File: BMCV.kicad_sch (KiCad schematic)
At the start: 30 parts, among them J13 DebugPins, J14 USB_C_Receptacle_USB2.0_14P, SW14 Reset, SW15 Boot, U32 TXS0108EPW, U36 STM32G474CETx, Y1 38.4MHz 10pF

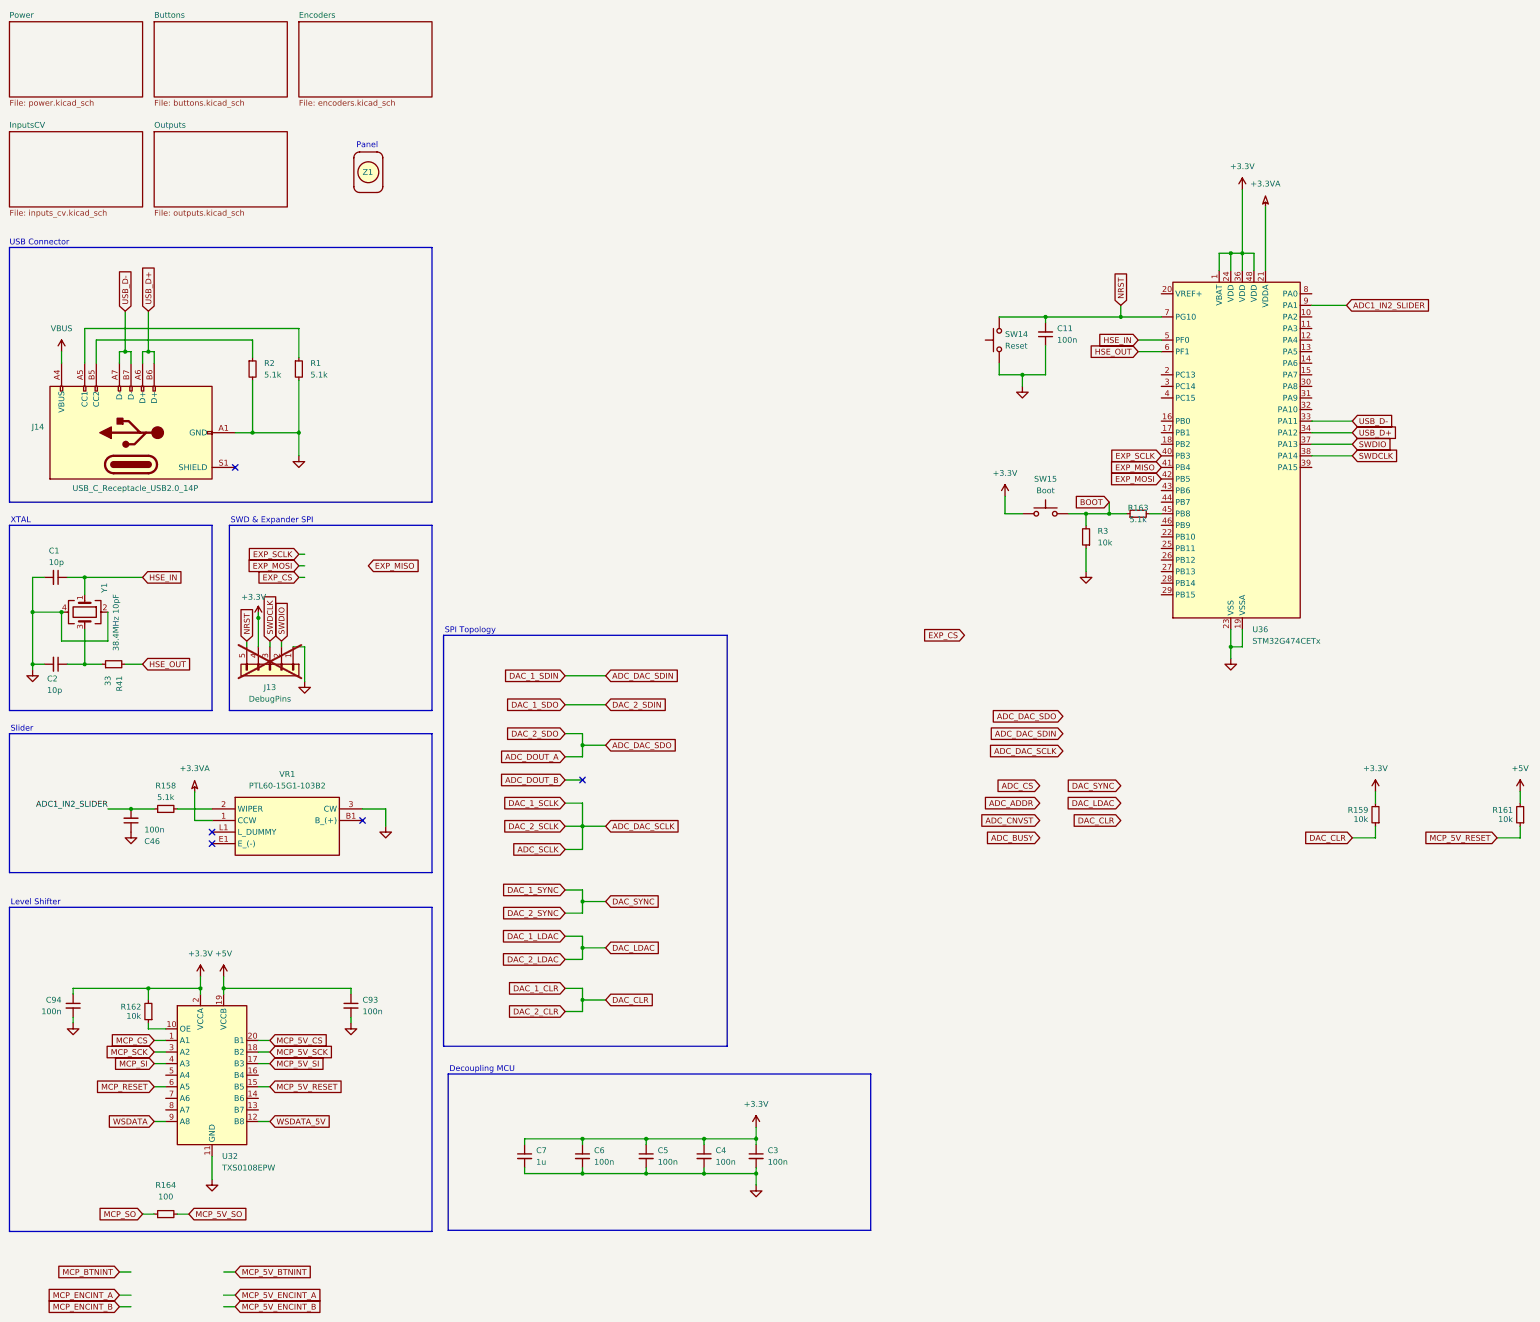
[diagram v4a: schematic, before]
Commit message: switches & led data routing
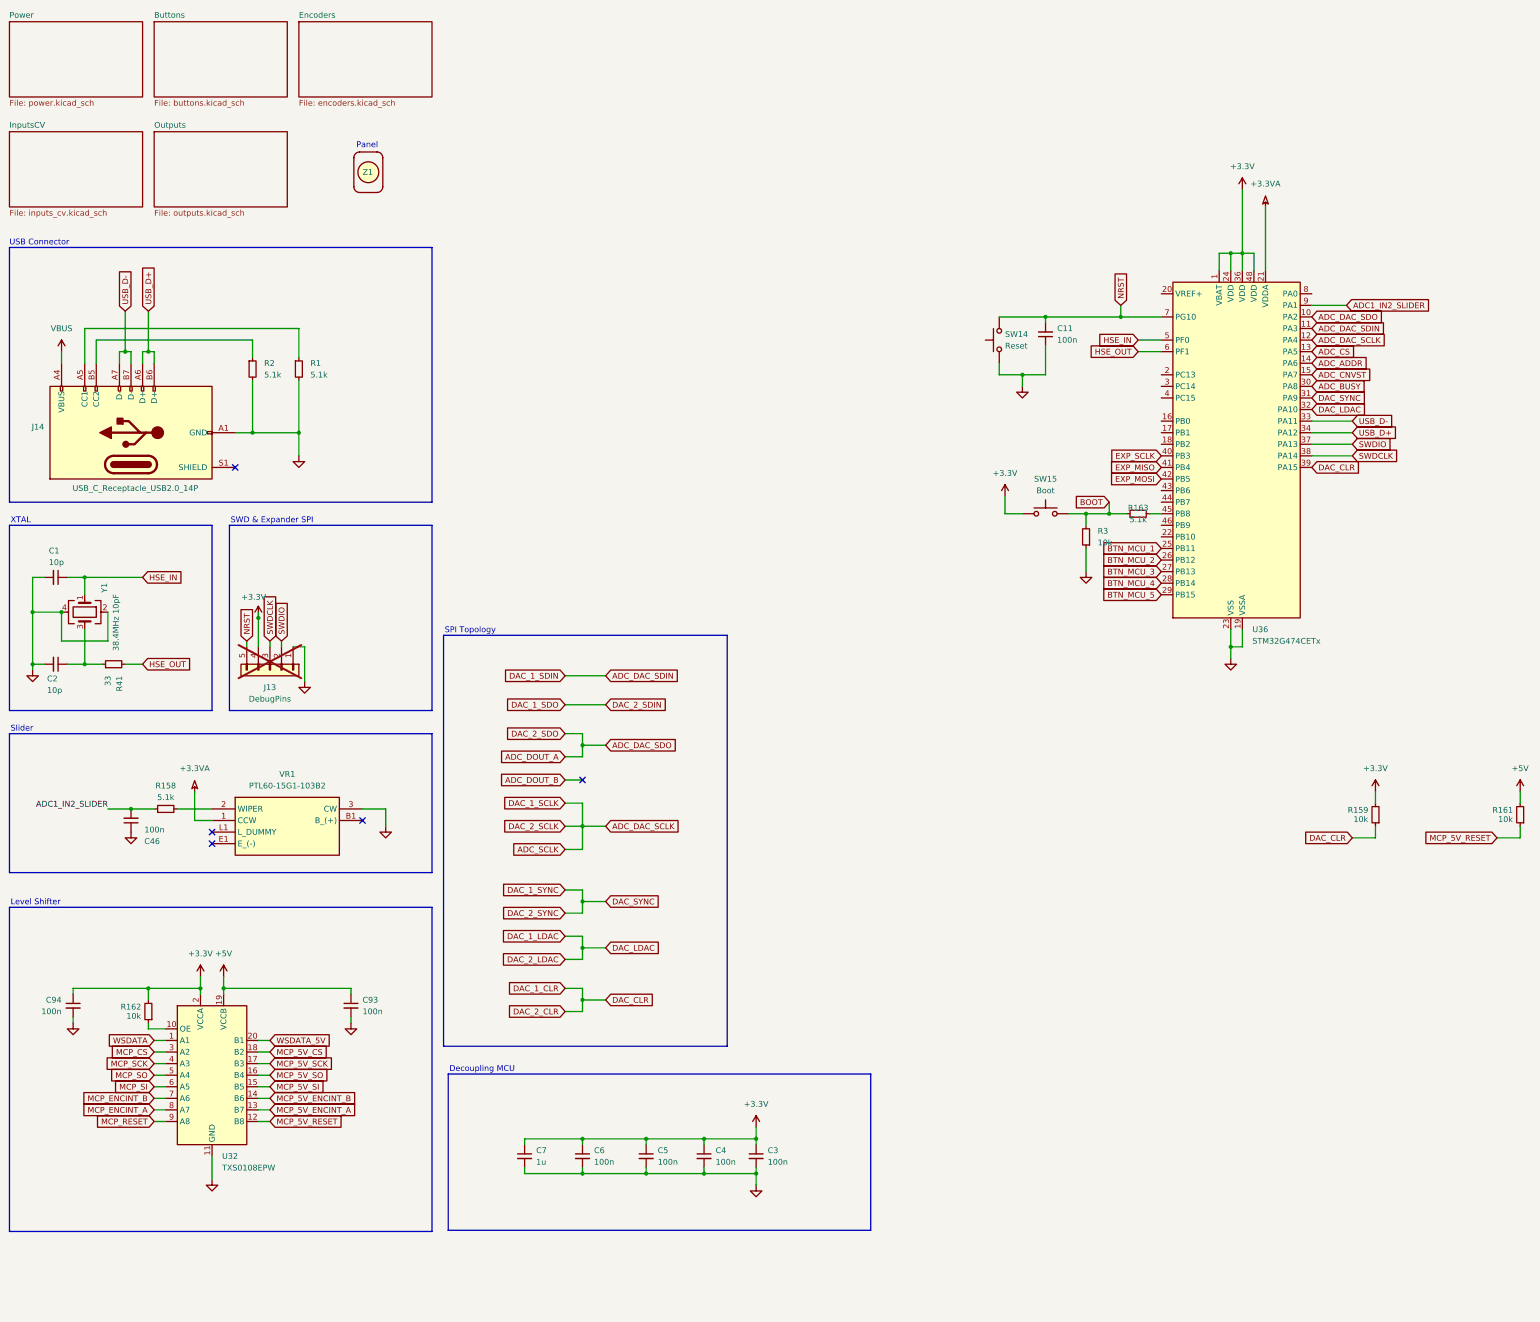
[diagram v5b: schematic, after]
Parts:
- removed R164: 100, Resistor_SMD:R_0603_1608Metric, symbol Device:R_Small
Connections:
- net ADC_ADDR: now also U36.14 (PA6)
- net ADC_BUSY: now also U36.30 (PA8)
- net ADC_CNVST: now also U36.15 (PA7)
- net ADC_CS: now also U36.13 (PA5)
- net ADC_DAC_SCLK: now also U36.12 (PA4)
- net ADC_DAC_SDIN: now also U36.11 (PA3)
- net ADC_DAC_SDO: now also U36.10 (PA2)
- net DAC_1_CLR: now also U36.39 (PA15)
- net DAC_1_LDAC: now also U36.32 (PA10)
- net DAC_1_SYNC: now also U36.31 (PA9)
- net MCP_5V_CS: now also U32.18 (B2); no longer U32.20 (B1)
- net MCP_5V_ENCINT_A: now also U32.13 (B7)
- net MCP_5V_ENCINT_B: now also U32.14 (B6)
- net MCP_5V_RESET: now also U32.12 (B8); no longer U32.15 (B5)
- net MCP_5V_SCK: now also U32.17 (B3); no longer U32.18 (B2)
- net MCP_5V_SI: now also U32.15 (B5); no longer U32.17 (B3)
- net MCP_5V_SO: now also U32.16 (B4)
- net MCP_CS: now also U32.3 (A2); no longer U32.1 (A1)
- net MCP_ENCINT_A: now also U32.8 (A7)
- net MCP_ENCINT_B: now also U32.7 (A6)
- net MCP_RESET: now also U32.9 (A8); no longer U32.6 (A5)
- net MCP_SCK: now also U32.4 (A3); no longer U32.3 (A2)
- net MCP_SI: now also U32.6 (A5); no longer U32.4 (A3)
- net MCP_SO: now also U32.5 (A4)
- net WSDATA: now also U32.1 (A1); no longer U32.9 (A8)
- net WSDATA_5V: now also U32.20 (B1); no longer U32.12 (B8)
- net BTN_MCU_1: now reaches U36.25 (PB11)
- net BTN_MCU_2: now reaches U36.26 (PB12)
- net BTN_MCU_3: now reaches U36.27 (PB13)
- net BTN_MCU_4: now reaches U36.28 (PB14)
- net BTN_MCU_5: now reaches U36.29 (PB15)

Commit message: completed routing and mcu pins
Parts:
- removed R41: 33, Resistor_SMD:R_0402_1005Metric, symbol Device:R_Small
- added C95: 100n, Capacitor_SMD:C_0402_1005Metric, symbol Device:C_Small
- added J15: Conn_01x02, TestPoint:TestPoint_2Pads_Pitch2.54mm_Drill0.8mm, symbol PCM_4ms_Connector:Conn_01x02
- added U37: MB85RS64PNF-G-JNERE1, Package_SO:SSOP-8_3.9x5.05mm_P1.27mm, symbol Memory_NVRAM:MB85RS64
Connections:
- net +3.3V: now also VR1.1 (CCW), C95.1, U37.3 (~{WP}), U37.7 (~{HOLD}), U37.8 (VDD)
- net +3.3VA: no longer VR1.1 (CCW)
- net ADC_ADDR: now also U36.25 (PB11); no longer U36.14 (PA6)
- net ADC_BUSY: now also U36.26 (PB12); no longer U36.30 (PA8)
- net ADC_CNVST: now also U36.22 (PB10); no longer U36.15 (PA7)
- net ADC_CS: now also U36.18 (PB2); no longer U36.13 (PA5)
- net ADC_DAC_SCLK: now also U36.27 (PB13); no longer U36.12 (PA4)
- net ADC_DAC_SDIN: now also U36.29 (PB15); no longer U36.11 (PA3)
- net ADC_DAC_SDO: now also U36.28 (PB14); no longer U36.10 (PA2)
- net BOOT: now also R163.2, U36.45 (PB8); no longer R163.1, R3.2, SW15.2
- net BTN_MCU_1: now also U36.46 (PB9); no longer U36.25 (PB11)
- net BTN_MCU_2: now also U36.2 (PC13); no longer U36.26 (PB12)
- net BTN_MCU_3: now also U36.8 (PA0); no longer U36.27 (PB13)
- net BTN_MCU_4: now also U36.4 (PC15); no longer U36.28 (PB14)
- net BTN_MCU_5: now also U36.3 (PC14); no longer U36.29 (PB15)
- net DAC_1_CLR: now also U36.30 (PA8); no longer U36.39 (PA15)
- net DAC_1_LDAC: now also U36.31 (PA9); no longer U36.32 (PA10)
- net DAC_1_SYNC: now also U36.32 (PA10); no longer U36.31 (PA9)
- net EXP_MISO: now also U37.2 (SO)
- net EXP_MOSI: now also U37.5 (SI)
- net EXP_SCLK: now also U37.6 (SCK)
- net GND: now also C95.2, U37.4 (GND)
- net HSE_OUT: now also C2.1, Y1.3
- net MCP_CS: now also U36.12 (PA4)
- net MCP_ENCINT_A: now also U36.10 (PA2)
- net MCP_ENCINT_B: now also U36.11 (PA3)
- net MCP_RESET: now also U36.16 (PB0)
- net MCP_SCK: now also U36.13 (PA5)
- net MCP_SI: now also U36.15 (PA7)
- net MCP_SO: now also U36.14 (PA6)
- net WSDATA: now also U36.17 (PB1)
- net PB6: now reaches U36.43 (PB6)
- net PB6: now also J15.1 (Pin_1)
- net PB7: now reaches U36.44 (PB7)
- net PB7: now also J15.2 (Pin_2)
- new net: R163.1, R3.2, SW15.2
- new net EXP_CS: U36.39 (PA15), U37.1 (~{CS})
- no-connect marks 5 -> 6
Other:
- note added: "Boot Switch"
- note added: "FRAM"
- note added: "Reset Switch"
- moved on the sheet: C11, R159, R161, R163, R3, SW14, SW15

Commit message: alpha
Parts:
- C1, C2: LCSC Part # (none) -> C32949
- C11, C3, C4, C46, C5, C6, C93, C94, C95: LCSC Part # (none) -> C307331
- C7: LCSC Part # (none) -> C15849
- J14: LCSC Part # (none) -> C22384784; now not fitted
- J15, VR1, Z1: now not fitted
- R1, R158, R163, R2: LCSC Part # (none) -> C25905
- R159, R161, R162, R3: LCSC Part # (none) -> C25744
- SW14, SW15: LCSC Part # (none) -> C2834959; now not fitted
- U32: LCSC Part # (none) -> C17206
- U36: LCSC Part # (none) -> C730125
- U37: LCSC Part # (none) -> C8741
- Y1: LCSC Part # (none) -> C3020671

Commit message: update
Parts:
- added C99: 100n, Capacitor_SMD:C_0402_1005Metric, symbol Device:C_Small
- J14, SW14, SW15, VR1, Z1: now fitted
- R1, R158, R2: value 5.1k -> 5k1
- R163: value 5.1k -> 100; LCSC Part # C25905 -> C25076
- R3: value 10k -> 5k1; LCSC Part # C25744 -> C25905
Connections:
- net GND: now also C99.1
- net at R163.1, R3.2, SW15.2: now also C99.2
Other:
- moved on the sheet: R163
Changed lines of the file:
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@@
 	)
 	(junction
+		(at 133.35 137.16)
+		(diameter 0)
+		(color 0 0 0 0)
+	)
+	(junction
 		(at 41.91 189.23)
 		(diameter 0)
@@
 	)
 	(junction
+		(at 137.16 127)
+		(diameter 0)
+		(color 0 0 0 0)
+	)
+	(junction
 		(at 140.97 269.24)
 		(diameter 0)
@@
 	(wire
 		(pts
-			(xy 133.35 134.62) (xy 133.35 139.7)
+			(xy 133.35 134.62) (xy 133.35 137.16)
 		)
 		(stroke
@@
 	(wire
 		(pts
+			(xy 137.16 134.62) (xy 137.16 137.16)
+		)
+		(stroke
+			(width 0)
+			(type default)
+		)
+	)
+	(wire
+		(pts
 			(xy 140.97 261.62) (xy 154.94 261.62)
 		)
@@
 	(wire
 		(pts
-			(xy 139.7 127) (xy 142.24 127)
+			(xy 137.16 127) (xy 139.065 127)
+		)
+		(stroke
+			(width 0)
+			(type default)
+		)
+	)
+	(wire
+		(pts
+			(xy 144.145 127) (xy 146.685 127)
 		)
 		(stroke
@@
 	(wire
 		(pts
+			(xy 133.35 137.16) (xy 133.35 139.7)
+		)
+		(stroke
+			(width 0)
+			(type default)
+		)
+	)
+	(wire
+		(pts
 			(xy 128.27 269.24) (xy 140.97 269.24)
 		)
@@
 	(wire
 		(pts
+			(xy 133.35 137.16) (xy 137.16 137.16)
+		)
+		(stroke
+			(width 0)
+			(type default)
+		)
+	)
+	(wire
+		(pts
 			(xy 140.97 261.62) (xy 140.97 262.89)
 		)
@@
 	(wire
 		(pts
-			(xy 133.35 127) (xy 134.62 127)
+			(xy 133.35 127) (xy 137.16 127)
 		)
 		(stroke
@@
 	(wire
 		(pts
+			(xy 137.16 127) (xy 137.16 129.54)
+		)
+		(stroke
+			(width 0)
+			(type default)
+		)
+	)
+	(wire
+		(pts
 			(xy 59.69 265.43) (xy 59.69 270.51)
 		)
@@
 	(global_label "BOOT"
 		(shape input)
-		(at 142.24 127 0)
+		(at 146.685 127 0)
 		(fields_autoplaced yes)
 		(effects
@@
 		)
 		(property "Intersheetrefs" "${INTERSHEET_REFS}"
-			(at 150.1238 127 0)
+			(at 154.5688 127 0)
 			(effects
 				(font
@@
 			)
 		)
-		(property "Value" "5.1k"
+		(property "Value" "5k1"
 			(at 81.28 93.9799 0)
 			(effects
@@
 	(symbol
 		(lib_id "Device:C_Small")
+		(at 137.16 132.08 180)
+		(unit 1)
+		(exclude_from_sim no)
+		(in_bom yes)
+		(on_board yes)
+		(dnp no)
+		(fields_autoplaced yes)
+		(property "Reference" "C99"
+			(at 139.7 130.8035 0)
+			(effects
+				(font
+					(size 1.27 1.27)
+				)
+				(justify right)
+			)
+		)
+		(property "Value" "100n"
+			(at 139.7 133.3435 0)
+			(effects
+				(font
+					(size 1.27 1.27)
+				)
+				(justify right)
+			)
+		)
+		(property "Footprint" "Capacitor_SMD:C_0402_1005Metric"
+			(at 137.16 132.08 0)
+			(effects
+				(font
+					(size 1.27 1.27)
+				)
+				(hide yes)
+			)
+		)
+		(property "Datasheet" "~"
+			(at 137.16 132.08 0)
+			(effects
+				(font
+					(size 1.27 1.27)
+				)
+				(hide yes)
+			)
+		)
+		(property "Description" "Multilayer Ceramic Capacitor (unpolarized)"
+			(at 137.16 132.08 0)
+			(effects
+				(font
+					(size 1.27 1.27)
+				)
+				(hide yes)
+			)
+		)
+		(property "LCSC Part #" "C307331"
+			(at 137.16 132.08 0)
+			(effects
+				(font
+					(size 1.27 1.27)
+				)
+				(hide yes)
+			)
+		)
+		(pin "1"
+		)
+		(pin "2"
+		)
+		(instances
+			(project "BMCV"
+				(path "/9b519346-c6ba-4bde-a176-1e9938a671fb"
+					(reference "C99")
+					(unit 1)
+				)
+			)
+		)
+	)
+	(symbol
+		(lib_id "Device:C_Small")
 		(at 41.91 191.77 180)
 		(unit 1)
@@
 		(in_bom yes)
 		(on_board yes)
-		(dnp yes)
+		(dnp no)
 		(fields_autoplaced yes)
 		(property "Reference" "SW14"
@@
 		(in_bom yes)
 		(on_board yes)
-		(dnp yes)
+		(dnp no)
 		(fields_autoplaced yes)
 		(property "Reference" "VR1"
@@
 		(in_bom no)
 		(on_board yes)
-		(dnp yes)
+		(dnp no)
 		(property "Reference" "Z1"
 			(at 92.71 49.53 0)
@@
 	(symbol
 		(lib_id "Device:R_Small")
-		(at 137.16 127 90)
+		(at 141.605 127 90)
 		(unit 1)
 		(exclude_from_sim no)
@@
 		(dnp no)
 		(property "Reference" "R163"
-			(at 137.16 122.428 90)
+			(at 141.605 122.428 90)
 			(effects
 				(font
@@
 			)
 		)
-		(property "Value" "5.1k"
-			(at 137.16 124.46 90)
+		(property "Value" "100"
+			(at 141.605 124.46 90)
 			(effects
 				(font
@@
 		)
 		(property "Footprint" "Resistor_SMD:R_0402_1005Metric"
-			(at 137.16 127 0)
+			(at 141.605 127 0)
 			(effects
 				(font
@@
 		)
 		(property "Datasheet" "~"
-			(at 137.16 127 0)
+			(at 141.605 127 0)
 			(effects
 				(font
@@
 		)
 		(property "Description" "Resistor, small symbol"
-			(at 137.16 127 0)
+			(at 141.605 127 0)
 			(effects
 				(font
@@
 			)
 		)
-		(property "LCSC Part #" "C25905"
-			(at 137.16 127 0)
+		(property "LCSC Part #" "C25076"
+			(at 141.605 127 0)
 			(effects
 				(font
@@
 			)
 		)
-		(property "Value" "5.1k"
+		(property "Value" "5k1"
 			(at 71.12 93.9799 0)
 			(effects
@@
 		(in_bom yes)
 		(on_board yes)
-		(dnp yes)
+		(dnp no)
 		(property "Reference" "J14"
 			(at 22.86 105.4099 90)
@@
 		(in_bom yes)
 		(on_board yes)
-		(dnp yes)
+		(dnp no)
 		(fields_autoplaced yes)
 		(property "Reference" "SW15"
@@
 			)
 		)
-		(property "Value" "5.1k"
+		(property "Value" "5k1"
 			(at 49.53 186.69 90)
 			(effects
@@
 			)
 		)
-		(property "Value" "10k"
+		(property "Value" "5k1"
 			(at 128.27 133.35 0)
 			(effects
@@
 			)
 		)
-		(property "LCSC Part #" "C25744"
+		(property "LCSC Part #" "C25905"
 			(at 133.35 132.08 0)
 			(effects
